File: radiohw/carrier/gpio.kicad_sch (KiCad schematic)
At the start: 6 parts, among them U10 PCA9555PW, U11 PCA9555PW, U7 PCA9555PW, U9 PCA9555PW

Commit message: Audio schematic development.
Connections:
- net MAIN_MUTE: now reaches U7.11 (IO0_7)
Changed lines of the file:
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@@
+    (stroke (width 0) (type default))
+  )
+  (wire (pts (xy 118.11 71.12) (xy 127 71.12))
     (stroke (width 0) (type default))
   )
@@
       (effects (font (size 1.27 1.27)) (justify left) hide)
     )
+  )
+  (global_label "MAIN_MUTE" (shape input) (at 127 71.12 0) (fields_autoplaced)
+    (effects (font (size 1.27 1.27)) (justify left))
+    (property "Intersheetrefs" "${INTERSHEET_REFS}" (at 140.3266 71.12 0)
+      (effects (font (size 1.27 1.27)) (justify left) hide)
+    )

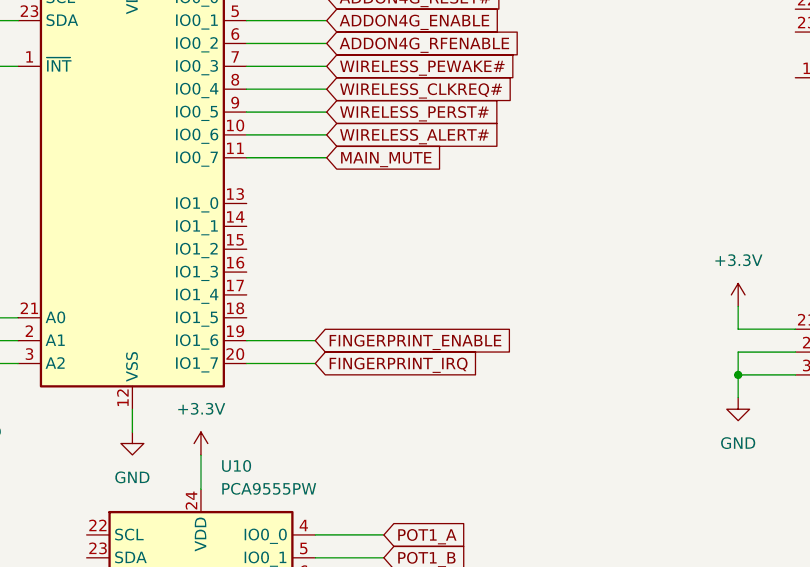
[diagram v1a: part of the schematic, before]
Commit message: Add accelerometer and i2c bus isolator to schematic.
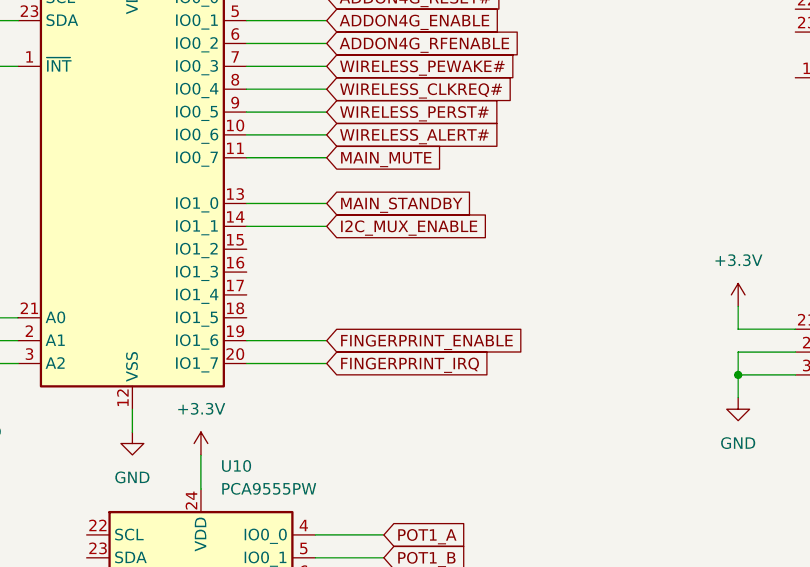
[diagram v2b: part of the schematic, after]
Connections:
- net MAIN_STANDBY: now reaches U7.13 (IO1_0)
- net I2C_MUX_ENABLE: now reaches U7.14 (IO1_1)
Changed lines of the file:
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@@
     (stroke (width 0) (type default))
   )
-  (wire (pts (xy 118.11 93.98) (xy 125.73 93.98))
+  (wire (pts (xy 118.11 93.98) (xy 127 93.98))
     (stroke (width 0) (type default))
   )
@@
     (stroke (width 0) (type default))
   )
-  (wire (pts (xy 118.11 91.44) (xy 125.73 91.44))
+  (wire (pts (xy 118.11 91.44) (xy 127 91.44))
     (stroke (width 0) (type default))
   )
@@
     (stroke (width 0) (type default))
   )
+  (wire (pts (xy 118.11 76.2) (xy 127 76.2))
+    (stroke (width 0) (type default))
+  )
   (wire (pts (xy 204.47 77.47) (xy 210.82 77.47))
     (stroke (width 0) (type default))
@@
   )
   (wire (pts (xy 125.73 143.51) (xy 133.35 143.51))
+    (stroke (width 0) (type default))
+  )
+  (wire (pts (xy 118.11 78.74) (xy 127 78.74))
     (stroke (width 0) (type default))
   )
@@
     )
   )
+  (global_label "MAIN_STANDBY" (shape input) (at 127 76.2 0) (fields_autoplaced)
+    (effects (font (size 1.27 1.27)) (justify left))
+    (property "Intersheetrefs" "${INTERSHEET_REFS}" (at 143.6529 76.2 0)
+      (effects (font (size 1.27 1.27)) (justify left) hide)
+    )
+  )
   (global_label "AUX4_OUT" (shape input) (at 210.82 95.25 0) (fields_autoplaced)
     (effects (font (size 1.27 1.27)) (justify left))
@@
     )
   )
+  (global_label "I2C_MUX_ENABLE" (shape input) (at 127 78.74 0) (fields_autoplaced)
+    (effects (font (size 1.27 1.27)) (justify left))
+    (property "Intersheetrefs" "${INTERSHEET_REFS}" (at 146.0113 78.74 0)
+      (effects (font (size 1.27 1.27)) (justify left) hide)
+    )
+  )
   (global_label "ADDON4G_ENABLE" (shape input) (at 127 55.88 0) (fields_autoplaced)
     (effects (font (size 1.27 1.27)) (justify left))
@@
     )
   )
-  (global_label "FINGERPRINT_IRQ" (shape input) (at 125.73 93.98 0) (fields_autoplaced)
-    (effects (font (size 1.27 1.27)) (justify left))
-    (property "Intersheetrefs" "${INTERSHEET_REFS}" (at 145.0439 93.98 0)
+  (global_label "FINGERPRINT_IRQ" (shape input) (at 127 93.98 0) (fields_autoplaced)
+    (effects (font (size 1.27 1.27)) (justify left))
+    (property "Intersheetrefs" "${INTERSHEET_REFS}" (at 146.3139 93.98 0)
       (effects (font (size 1.27 1.27)) (justify left) hide)
     )
@@
     )
   )
-  (global_label "FINGERPRINT_ENABLE" (shape input) (at 125.73 91.44 0) (fields_autoplaced)
-    (effects (font (size 1.27 1.27)) (justify left))
-    (property "Intersheetrefs" "${INTERSHEET_REFS}" (at 148.8538 91.44 0)
-      (effects (font (size 1.27 1.27)) (justify left) hide)
-    )
+  (global_label "FINGERPRINT_ENABLE" (shape input) (at 127 91.44 0) (fields_autoplaced)
+    (effects (font (size 1.27 1.27)) (justify left))
+    (property "Intersheetrefs" "${INTERSHEET_REFS}" (at 150.1238 91.44 0)
+      (effects (font (size 1.27 1.27)) (justify left) hide)
+    )
